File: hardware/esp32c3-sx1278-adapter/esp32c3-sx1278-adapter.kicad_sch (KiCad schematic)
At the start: 5 parts, among them J1 Conn_01x08, J2 Conn_01x08, J3 Antenna, J4 SMA, U2 SX1278_module

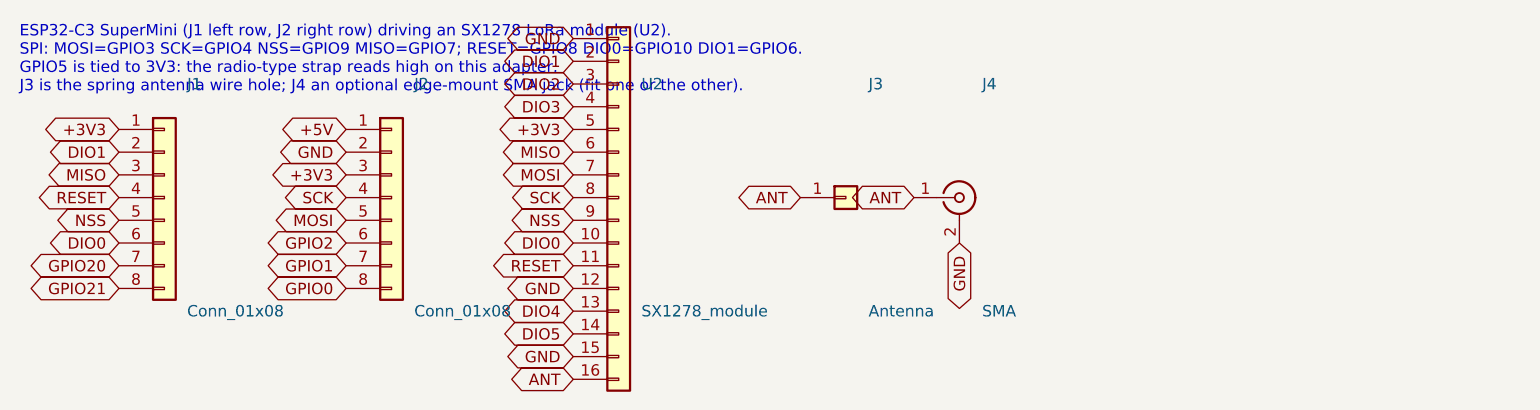
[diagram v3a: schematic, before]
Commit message: SX1278 module adapter: move NSS and RESET off the GPIO8/GPIO9 straps
Same boot-strap hazard as the socket adapter: the module's NSS sat on GPIO9
(the BOOT strap) and RESET on GPIO8, so at reset the module's pin capacitance
could hold a strap low through the weak internal pull-up and drop the chip
into USB download mode.  On this two-layer board the fix keeps the nested
front-copper left bus by shifting the chain: NSS GPIO9 -> GPIO10, DIO0
GPIO10 -> GPIO20, RESET GPIO8 -> GPIO21, so the pad order still matches the
pin order and no lane crosses.  GPIO8 and GPIO9 are now unused.  The old
bottom-copper RESET run is removed.  README and schematic note updated;
ERC/DRC clean.

Co-Authored-By: Claude Opus 4.8 <noreply@anthropic.com>
Claude-Session: https://claude.ai/code/session_01JoGdh4Cg3VtTTDZi4gQuiN
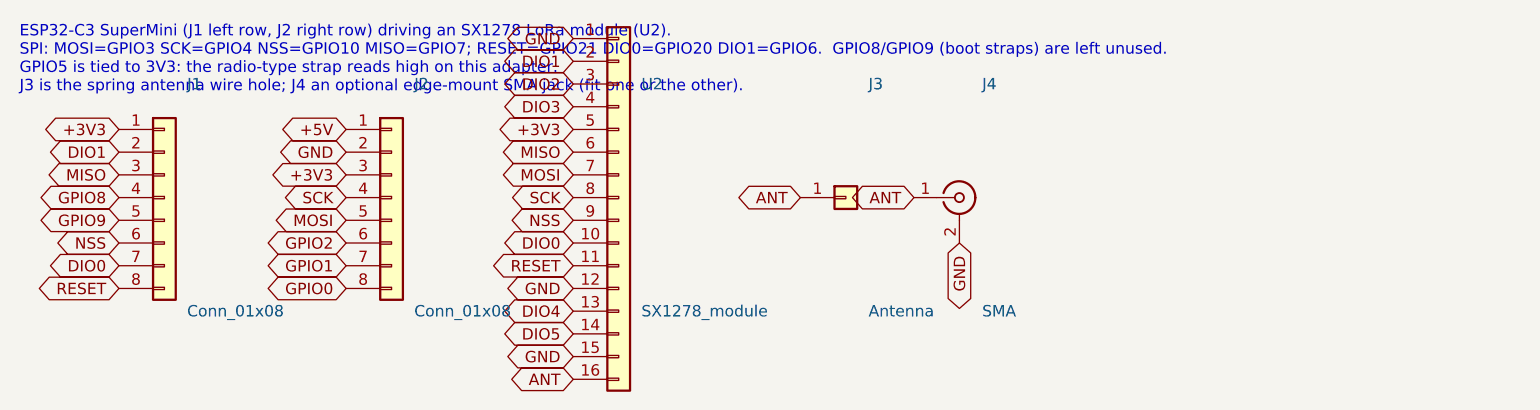
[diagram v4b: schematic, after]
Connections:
- net GPIO20 is gone; now on net DIO0: J1.7 (Pin_7)
- net GPIO21 is gone; now on net RESET: J1.8 (Pin_8)
- net DIO0: no longer J1.6 (Pin_6)
- net NSS: now also J1.6 (Pin_6); no longer J1.5 (Pin_5)
- net RESET: no longer J1.4 (Pin_4)
- new net GPIO8: J1.4 (Pin_4)
- new net GPIO9: J1.5 (Pin_5)
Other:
- note added: "ESP32-C3 SuperMini (J1 left row, J2 right row) driving an SX1278 LoRa module (U2). SPI: MOSI=GPIO3 SCK=GPIO4 NSS=GPIO10 MISO=GPIO7; RESET=GPIO21 DIO0=GPIO20 DIO1=GPIO6. GPIO8/GPIO9 (boot straps) are left unused. GPIO5 is tied to 3V3: the radio-type strap reads high on this adapter. J3 is the spring antenna wire hole; J4 an optional edge-mount SMA jack (fit one or the other)."
- note removed: "ESP32-C3 SuperMini (J1 left row, J2 right row) driving an SX1278 LoRa module (U2). SPI: MOSI=GPIO3 SCK=GPIO4 NSS=GPIO9 MISO=GPIO7; RESET=GPIO8 DIO0=GPIO10 DIO1=GPIO6. GPIO5 is tied to 3V3: the radio-type strap reads high on this adapter. J3 is the spring antenna wire hole; J4 an optional edge-mount SMA jack (fit one or the other)."
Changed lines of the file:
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@@
+		)
+	)
+	(global_label "GPIO8"
+		(shape bidirectional)
+		(at 71.12 101.6 180)
+		(fields_autoplaced yes)
+		(effects
+			(font
+				(size 1.27 1.27)
+			)
+			(justify right)
+		)
+		(property "Intersheetrefs" "${INTERSHEET_REFS}"
+			(at 71.12 101.6 0)
+			(effects
+				(font
+					(size 1.27 1.27)
+				)
+				(justify right)
+				(hide yes)
+			)
+		)
+	)
+	(global_label "GPIO9"
+		(shape bidirectional)
+		(at 71.12 104.14 180)
+		(fields_autoplaced yes)
+		(effects
+			(font
+				(size 1.27 1.27)
+			)
+			(justify right)
+		)
+		(property "Intersheetrefs" "${INTERSHEET_REFS}"
+			(at 71.12 104.14 0)
+			(effects
+				(font
+					(size 1.27 1.27)
+				)
+				(justify right)
+				(hide yes)
+			)
+		)
+	)
+	(global_label "NSS"
+		(shape bidirectional)
+		(at 71.12 106.68 180)
+		(fields_autoplaced yes)
+		(effects
+			(font
+				(size 1.27 1.27)
+			)
+			(justify right)
+		)
+		(property "Intersheetrefs" "${INTERSHEET_REFS}"
+			(at 71.12 106.68 0)
+			(effects
+				(font
+					(size 1.27 1.27)
+				)
+				(justify right)
+				(hide yes)
+			)
+		)
+	)
+	(global_label "DIO0"
+		(shape bidirectional)
+		(at 71.12 109.22 180)
+		(fields_autoplaced yes)
+		(effects
+			(font
+				(size 1.27 1.27)
+			)
+			(justify right)
+		)
+		(property "Intersheetrefs" "${INTERSHEET_REFS}"
+			(at 71.12 109.22 0)
+			(effects
+				(font
+					(size 1.27 1.27)
+				)
+				(justify right)
+				(hide yes)
+			)
 		)
 	)
 	(global_label "RESET"
-		(shape bidirectional)
-		(at 71.12 101.6 180)
-		(fields_autoplaced yes)
-		(effects
-			(font
-				(size 1.27 1.27)
-			)
-			(justify right)
-		)
-		(property "Intersheetrefs" "${INTERSHEET_REFS}"
-			(at 71.12 101.6 0)
-			(effects
-				(font
-					(size 1.27 1.27)
-				)
-				(justify right)
-				(hide yes)
-			)
-		)
-	)
-	(global_label "NSS"
-		(shape bidirectional)
-		(at 71.12 104.14 180)
-		(fields_autoplaced yes)
-		(effects
-			(font
-				(size 1.27 1.27)
-			)
-			(justify right)
-		)
-		(property "Intersheetrefs" "${INTERSHEET_REFS}"
-			(at 71.12 104.14 0)
-			(effects
-				(font
-					(size 1.27 1.27)
-				)
-				(justify right)
-				(hide yes)
-			)
-		)
-	)
-	(global_label "DIO0"
-		(shape bidirectional)
-		(at 71.12 106.68 180)
-		(fields_autoplaced yes)
-		(effects
-			(font
-				(size 1.27 1.27)
-			)
-			(justify right)
-		)
-		(property "Intersheetrefs" "${INTERSHEET_REFS}"
-			(at 71.12 106.68 0)
-			(effects
-				(font
-					(size 1.27 1.27)
-				)
-				(justify right)
-				(hide yes)
-			)
-		)
-	)
-	(global_label "GPIO20"
-		(shape bidirectional)
-		(at 71.12 109.22 180)
-		(fields_autoplaced yes)
-		(effects
-			(font
-				(size 1.27 1.27)
-			)
-			(justify right)
-		)
-		(property "Intersheetrefs" "${INTERSHEET_REFS}"
-			(at 71.12 109.22 0)
-			(effects
-				(font
-					(size 1.27 1.27)
-				)
-				(justify right)
-				(hide yes)
-			)
-		)
-	)
-	(global_label "GPIO21"
 		(shape bidirectional)
 		(at 71.12 111.76 180)
@@
 		)
 	)
-	(text "ESP32-C3 SuperMini (J1 left row, J2 right row) driving an SX1278 LoRa module (U2).\nSPI: MOSI=GPIO3 SCK=GPIO4 NSS=GPIO9 MISO=GPIO7; RESET=GPIO8 DIO0=GPIO10 DIO1=GPIO6.\nGPIO5 is tied to 3V3: the radio-type strap reads high on this adapter.\nJ3 is the spring antenna wire hole; J4 an optional edge-mount SMA jack (fit one or the other)."
+	(text "ESP32-C3 SuperMini (J1 left row, J2 right row) driving an SX1278 LoRa module (U2).\nSPI: MOSI=GPIO3 SCK=GPIO4 NSS=GPIO10 MISO=GPIO7; RESET=GPIO21 DIO0=GPIO20 DIO1=GPIO6.  GPIO8/GPIO9 (boot straps) are left unused.\nGPIO5 is tied to 3V3: the radio-type strap reads high on this adapter.\nJ3 is the spring antenna wire hole; J4 an optional edge-mount SMA jack (fit one or the other)."
 		(exclude_from_sim no)
 		(at 60 90 0)
